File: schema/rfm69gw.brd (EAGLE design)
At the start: 59.9 x 37.1 mm, 18 parts, among them IC1 ESP-12-SMD, IC2 AMS1117-3.3, U1 RFM69CW

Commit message: Board images
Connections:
- removed net GND4: X1.GND@1
- net GND: now also X1.GND@1
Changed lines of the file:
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@@
 <via x="16.764" y="34.29" extent="1-16" drill="0.6"/>
 <contactref element="JP3" pad="2"/>
+<contactref element="X1" pad="GND@1"/>
 </signal>
 <signal name="RESET">
@@
 <wire x1="51.308" y1="8.056" x2="51.308" y2="10.16" width="0.4064" layer="1"/>
 </signal>
-<signal name="GND4">
-<contactref element="X1" pad="GND@1"/>
-</signal>
 <signal name="N$1">

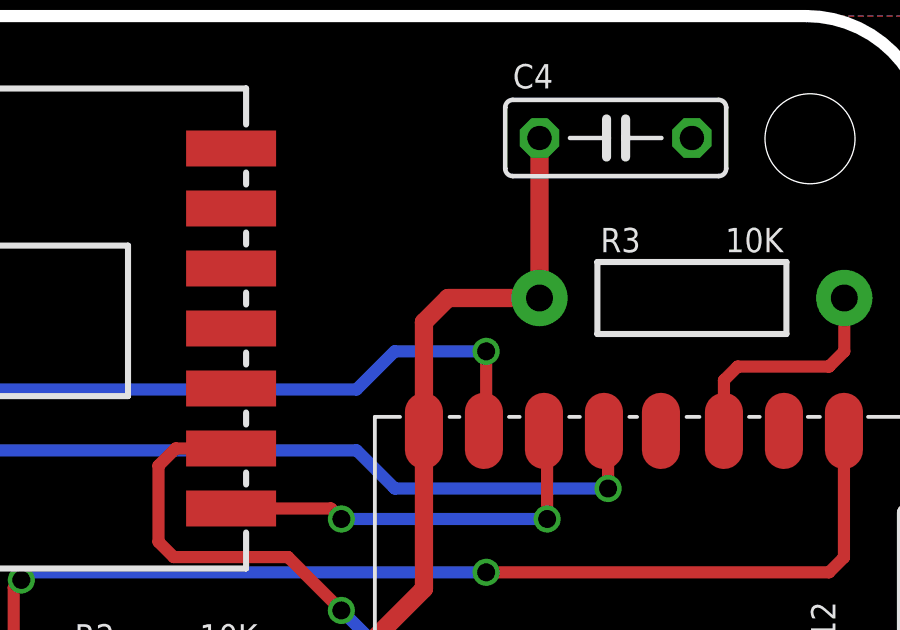
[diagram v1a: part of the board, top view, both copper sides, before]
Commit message: Schema updated
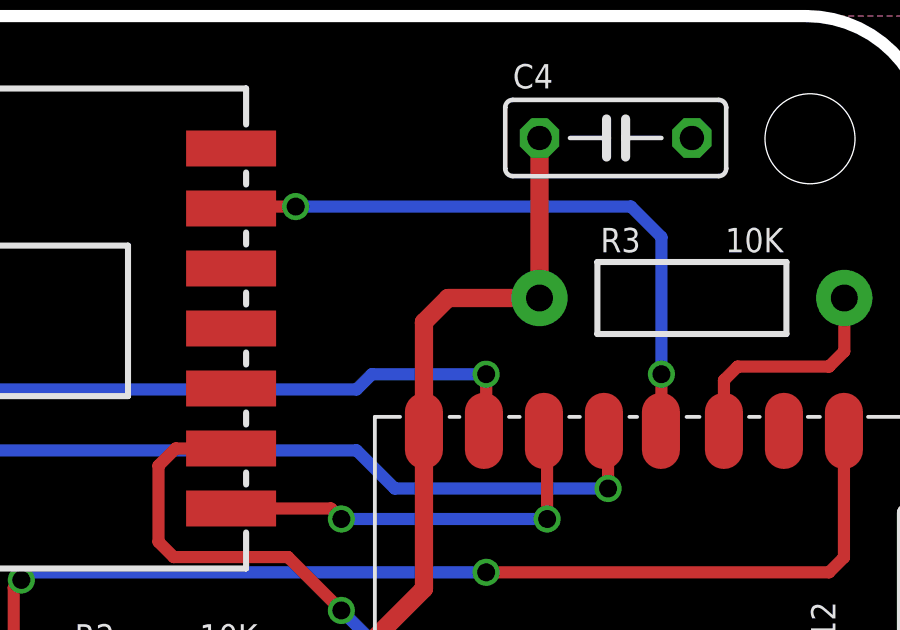
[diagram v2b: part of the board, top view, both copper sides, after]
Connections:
- new net RST: IC1.GPIO16, U1.13
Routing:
- net RST: track 0.00 -> 21.3 mm, vias 0 -> 2
- net MOSI: track 27.1 -> 26.1 mm
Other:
- board text added: "Tinkerman 2016 RFM69 GATEWAY 0.4.20160829"
- board text removed: "Tinkerman 2016 RFM69 GATEWAY 0.3.20160731"
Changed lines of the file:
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@@
 <text x="29.718" y="29.21" size="0.8128" layer="22" font="vector" ratio="15" rot="MR0" align="center">Tinkerman 2016
 RFM69 GATEWAY
-0.3.20160731</text>
+0.4.20160829</text>
 <text x="47.752" y="4.572" size="0.8128" layer="21" font="vector" ratio="15" align="bottom-center">IO5</text>
 </plain>
@@
 <via x="24.892" y="24.638" extent="1-16" drill="0.6"/>
 <wire x1="24.892" y1="24.638" x2="41.148" y2="24.638" width="0.4064" layer="16"/>
-<wire x1="41.148" y1="24.638" x2="42.418" y2="25.908" width="0.4064" layer="16"/>
-<wire x1="42.418" y1="25.908" x2="45.466" y2="25.908" width="0.4064" layer="16"/>
-<via x="45.466" y="25.908" extent="1-16" drill="0.6"/>
-<wire x1="45.466" y1="25.908" x2="45.466" y2="23.33" width="0.4064" layer="1"/>
+<wire x1="41.148" y1="24.638" x2="41.656" y2="25.146" width="0.4064" layer="16"/>
+<wire x1="41.656" y1="25.146" x2="45.466" y2="25.146" width="0.4064" layer="16"/>
+<via x="45.466" y="25.146" extent="1-16" drill="0.6"/>
+<wire x1="45.466" y1="25.146" x2="45.466" y2="23.33" width="0.4064" layer="1"/>
 <wire x1="45.466" y1="23.33" x2="45.392" y2="23.256" width="0.4064" layer="1"/>
 <wire x1="21.964" y1="24.67" x2="21.558" y2="24.67" width="0.4064" layer="1"/>
@@
 <wire x1="50.8" y1="6.35" x2="47.752" y2="3.302" width="0.4064" layer="1"/>
 </signal>
+<signal name="RST">
+<contactref element="U1" pad="13"/>
+<contactref element="IC1" pad="GPIO16"/>
+<wire x1="51.292" y1="23.256" x2="51.308" y2="23.256" width="0.4064" layer="1"/>
+<wire x1="51.308" y1="23.256" x2="51.308" y2="25.146" width="0.4064" layer="1"/>
+<via x="51.308" y="25.146" extent="1-16" drill="0.6"/>
+<via x="39.116" y="30.734" extent="1-16" drill="0.6"/>
+<wire x1="39.116" y1="30.734" x2="37.028" y2="30.734" width="0.4064" layer="1"/>
+<wire x1="37.028" y1="30.734" x2="36.964" y2="30.67" width="0.4064" layer="1"/>
+<wire x1="51.308" y1="25.146" x2="51.308" y2="29.718" width="0.4064" layer="16"/>
+<wire x1="51.308" y1="29.718" x2="50.292" y2="30.734" width="0.4064" layer="16"/>
+<wire x1="50.292" y1="30.734" x2="39.116" y2="30.734" width="0.4064" layer="16"/>
+</signal>
 </signals>

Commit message: Small changes in the gateway layout
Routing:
- net RST: vias 2 -> 0
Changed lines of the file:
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@@
 <?xml version="1.0" encoding="utf-8"?>
 <!DOCTYPE eagle SYSTEM "eagle.dtd">
-<eagle version="7.3.0">
+<eagle version="8.2.1">
 <drawing>
 <settings>
@@
 <elements>
 <element name="IC2" library="xose" package="SOT223" value="AMS1117-3.3" x="4.699" y="23.495">
+<attribute name="MF" value="" x="4.699" y="23.495" size="1.778" layer="27" display="off"/>
+<attribute name="MPN" value="REG1117" x="4.699" y="23.495" size="1.778" layer="27" display="off"/>
+<attribute name="OC_FARNELL" value="1097566" x="4.699" y="23.495" size="1.778" layer="27" display="off"/>
 <attribute name="OC_NEWARK" value="14P6981" x="4.699" y="23.495" size="1.778" layer="27" display="off"/>
-<attribute name="OC_FARNELL" value="1097566" x="4.699" y="23.495" size="1.778" layer="27" display="off"/>
-<attribute name="MPN" value="REG1117" x="4.699" y="23.495" size="1.778" layer="27" display="off"/>
-<attribute name="MF" value="" x="4.699" y="23.495" size="1.778" layer="27" display="off"/>
 </element>
 <element name="R1" library="xose" package="AXIAL-0.4" value="10K" x="34.798" y="9.906"/>
@@
 <wire x1="43.392" y1="26.882" x2="44.196" y2="27.686" width="0.6096" layer="1"/>
 <wire x1="44.196" y1="27.686" x2="47.244" y2="27.686" width="0.6096" layer="1"/>
-<wire x1="47.244" y1="27.686" x2="47.244" y2="33.02" width="0.6096" layer="1"/>
+<wire x1="47.244" y1="27.686" x2="47.244" y2="33.02" width="0.6096" layer="16"/>
 <wire x1="9.398" y1="28.575" x2="18.923" y2="28.575" width="0.6096" layer="1"/>
 <wire x1="18.923" y1="28.575" x2="19.558" y2="29.21" width="0.6096" layer="1"/>
@@
 <contactref element="IC1" pad="GPIO16"/>
 <wire x1="51.292" y1="23.256" x2="51.308" y2="23.256" width="0.4064" layer="1"/>
-<wire x1="51.308" y1="23.256" x2="51.308" y2="25.146" width="0.4064" layer="1"/>
-<via x="51.308" y="25.146" extent="1-16" drill="0.6"/>
-<via x="39.116" y="30.734" extent="1-16" drill="0.6"/>
-<wire x1="39.116" y1="30.734" x2="37.028" y2="30.734" width="0.4064" layer="1"/>
 <wire x1="37.028" y1="30.734" x2="36.964" y2="30.67" width="0.4064" layer="1"/>
-<wire x1="51.308" y1="25.146" x2="51.308" y2="29.718" width="0.4064" layer="16"/>
-<wire x1="51.308" y1="29.718" x2="50.292" y2="30.734" width="0.4064" layer="16"/>
-<wire x1="50.292" y1="30.734" x2="39.116" y2="30.734" width="0.4064" layer="16"/>
+<wire x1="51.308" y1="23.256" x2="51.308" y2="29.718" width="0.4064" layer="1"/>
+<wire x1="51.308" y1="29.718" x2="50.292" y2="30.734" width="0.4064" layer="1"/>
+<wire x1="50.292" y1="30.734" x2="37.028" y2="30.734" width="0.4064" layer="1"/>
 </signal>
 </signals>
